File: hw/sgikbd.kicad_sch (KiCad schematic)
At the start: 31 parts, among them J1 AVR-ISP, Q1 2N7002, SW1 RESET, U1 ATmega328PB, U2 ps2kbd, U3 ps2aux, U4 LM358, U5 sgi-mdin6, U6 L7805, U7 L7905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

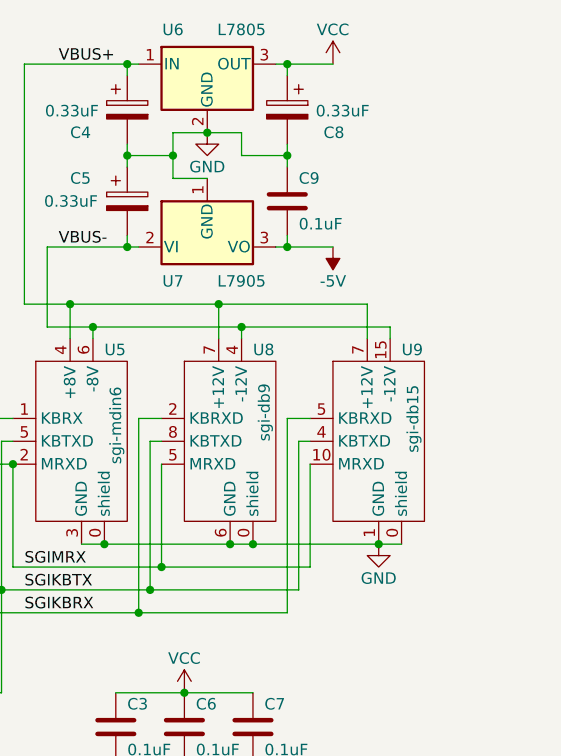
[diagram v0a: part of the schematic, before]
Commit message: rev3: jumper-selectable R3K hack
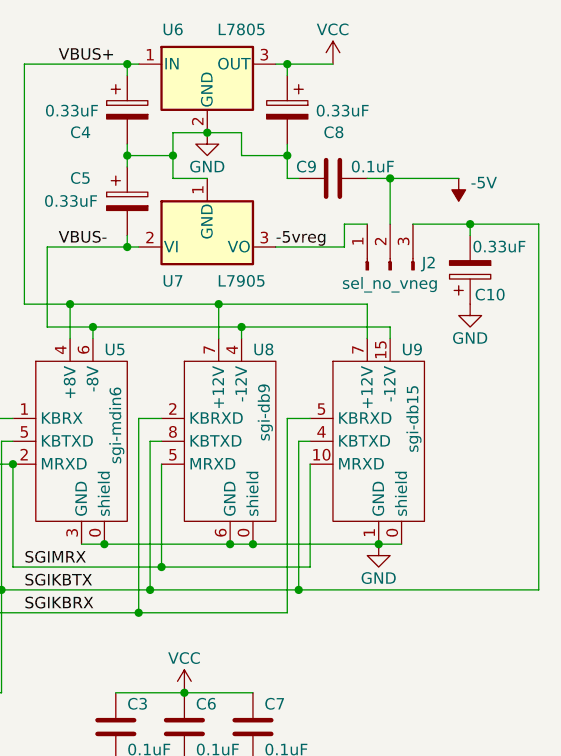
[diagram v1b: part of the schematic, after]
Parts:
- added C10: 0.33uF, Capacitor_SMD:CP_Elec_4x5.4, symbol Device:C_Polarized
- added J2: sel_no_vneg, Connector_PinHeader_2.54mm:PinHeader_1x03_P2.54mm_Vertical, symbol Connector:Conn_01x03_Pin
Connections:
- net -5V: now also J2.2 (Pin_2); no longer U7.3 (VO)
- net GND: now also C10.1
- net SGIKBTX: now also C10.2, J2.3 (Pin_3)
- new net -5vreg: J2.1 (Pin_1), U7.3 (VO)
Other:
- moved on the sheet: C9
